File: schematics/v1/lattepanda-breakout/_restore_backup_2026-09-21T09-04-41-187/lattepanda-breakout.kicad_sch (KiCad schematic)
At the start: 10 parts, among them J1 RJ45, J2 SDI12, J3 SDI12, J4 Conn_02x04_Odd_Even, J5 Conn_02x15_Odd_Even, J6 Conn_02x02_Odd_Even, U1 MAX22508

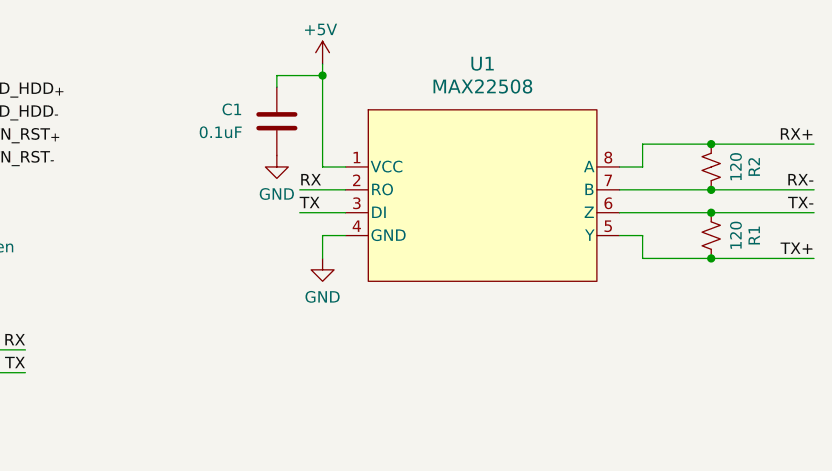
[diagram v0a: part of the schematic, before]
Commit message: update(lattepanda-breakout): rev2
added rs485 connection
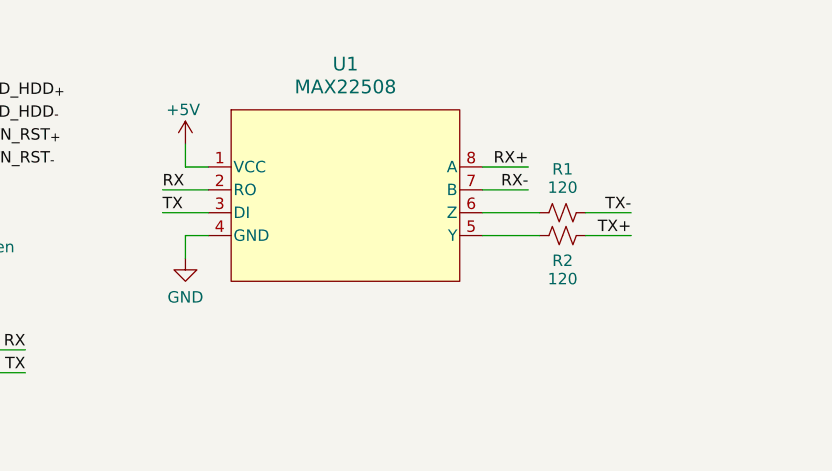
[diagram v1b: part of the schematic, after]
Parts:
- removed C1: 0.1uF, symbol Device:C
- J2, J3: footprint Link_Footprints:PC-1053866 -> Link_Footprints:PC-1818517
- J5: footprint Connector_PinHeader_2.54mm:PinHeader_2x15_P2.54mm_Vertical_SMD -> Connector_PinHeader_2.54mm:PinHeader_2x15_P2.54mm_Vertical
- J6: footprint Connector_PinHeader_2.54mm:PinHeader_2x02_P2.54mm_Vertical_SMD -> Connector_PinHeader_2.54mm:PinHeader_2x02_P2.54mm_Vertical
- R1, R2: footprint Resistor_SMD:R_0805_2012Metric -> (none)
- U1: footprint Link_Footprints:MAX22508 -> 21-0041_S8+2C_MXM
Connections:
- net RX+: no longer R2.2
- net RX-: no longer R2.1
- net TX+: now also R2.2; no longer R1.2, U1.5 (Y)
- net TX-: now also R1.2; no longer R1.1, U1.6 (Z)
- new net: R2.1, U1.5 (Y)
- new net: R1.1, U1.6 (Z)
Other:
- moved on the sheet: R1, U1
